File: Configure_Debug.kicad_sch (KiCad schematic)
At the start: 0 parts

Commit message: 更换电阻至新的结构
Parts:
- added CN5: 3020-10-0300-00-TR, MY_Connector_PH2.54:CONN_3020-10-0300-00-TR_CNC, symbol MY_Connector:3020-10-0300-00-TR
- added S1: 100mA 25VDC, MY_Switch:CK_SW_SD08H0SBR, symbol MY_Switch:SD08H0SBR
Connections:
- new net FULLPWRMGMTZ_SMBA1: S1.1
- new net GANGED_SMBA2_HS: S1.4
- new net PWRCTL_POL_TDO: S1.2
- new net PWRCTRL_BATEN1: S1.7
- new net PWRCTRL_BATEN2: S1.8
- new net SCL_SMBCLK: S1.5
- new net SDA_SMBDAT: S1.6
- new net SMBUSZ: S1.3

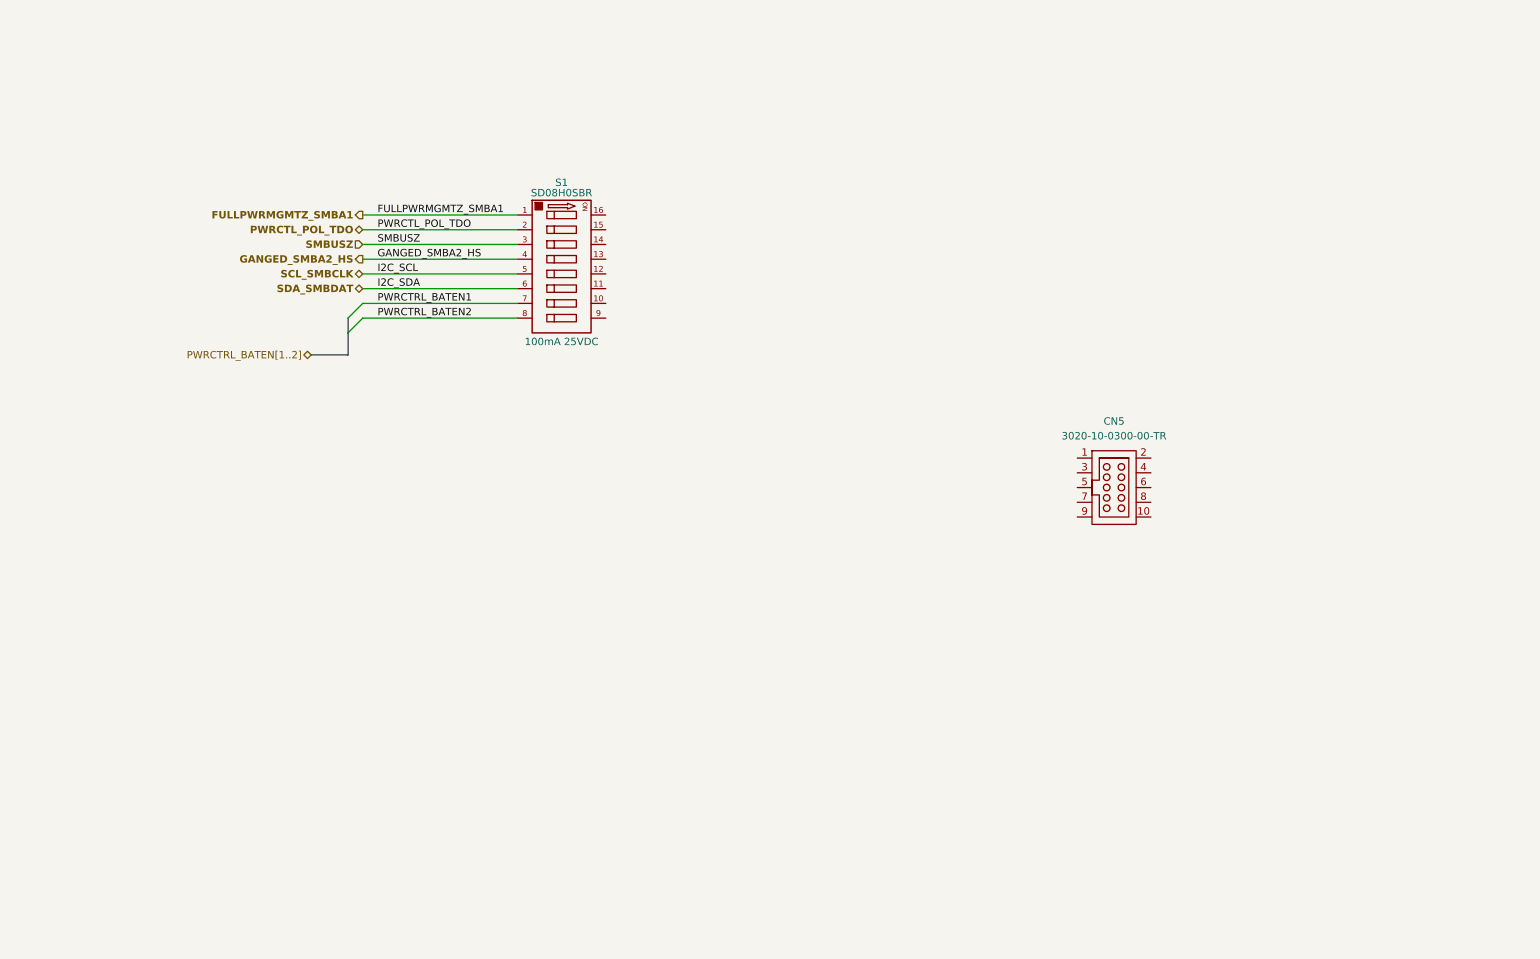
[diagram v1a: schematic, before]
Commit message: 完成电路原理图的绘制与批注
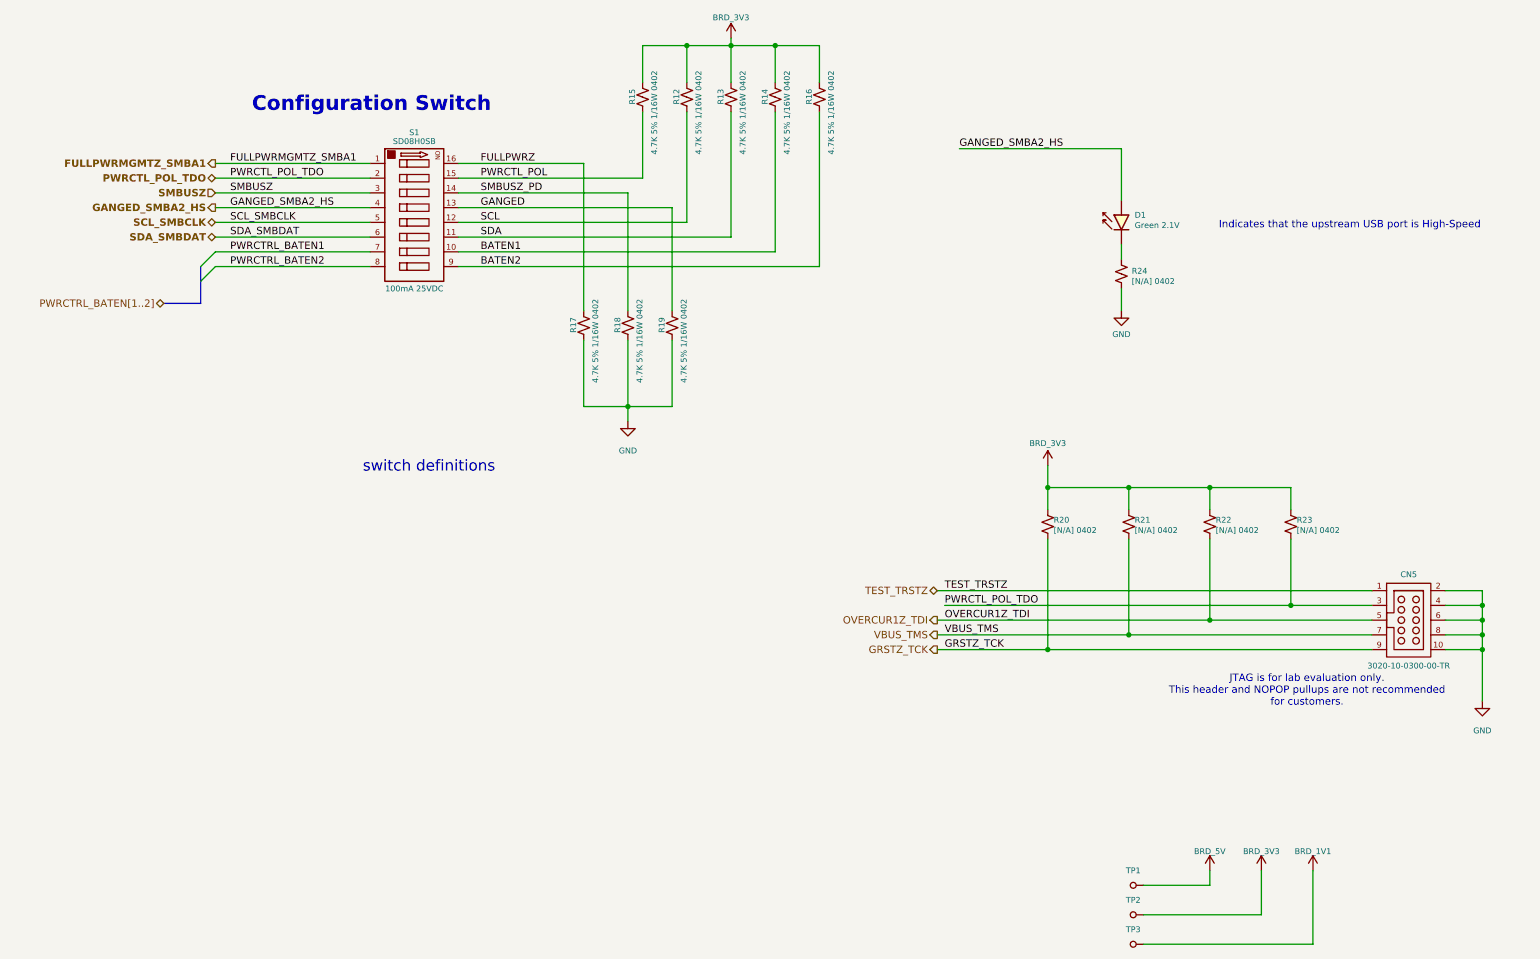
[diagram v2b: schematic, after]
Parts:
- removed CN5: 3020-10-0300-00-TR, MY_Connector_PH2.54:CONN_3020-10-0300-00-TR_CNC, symbol MY_Connector:3020-10-0300-00-TR
- removed S1: 100mA 25VDC, MY_Switch:CK_SW_SD08H0SBR, symbol MY_Switch:SD08H0SBR
- added CN5: 3020-10-0300-00-TR, MY_Connector_PH2.54:CONN_3020-10-0300-00-TR_CNC, symbol MY_CONN_PH2.54mm:3020-10-0300-00-TR
- added D1: Green 2.1V, MY_Led:LTST-C171, symbol MY_Led:LTST-C171GKT
- added R12, R13, R14, R15, R16, R17, R18, R19: 4.7K 5% 1/16W 0402, MY_Res:YAGEO_R0402, symbol MY_Res_YAGEO_AF:AF0402JR-074K7L
- added R20, R21, R22, R23, R24: [N/A] 0402, MY_Res:YAGEO_R0402, symbol MY_Res_YAGEO_AF:AF0402XXXXXXXXXL
- added S1: 100mA 25VDC, MY_Switch:CK_SW_SD08H0SB, symbol MY_Switch:SD08H0SB
- added TP1, TP2, TP3: ~, MY_Test:TP_Pad_D1.5mm, symbol MY_Test:TP_Pad_D1.5mm
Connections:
- net FULLPWRMGMTZ_SMBA1: now also S1.1
- net GANGED_SMBA2_HS: now also D1.2 (A), S1.4
- net PWRCTL_POL_TDO: now also CN5.3, R23.2, S1.2
- net PWRCTRL_BATEN1: now also S1.7
- net PWRCTRL_BATEN2: now also S1.8
- net SCL_SMBCLK: now also S1.5
- net SDA_SMBDAT: now also S1.6
- net SMBUSZ: now also S1.3
- new net: D1.1 (K), R24.1
- new net BATEN1: R14.2, S1.10
- new net BATEN2: R16.2, S1.9
- new net BRD_1V1: TP3.1
- new net BRD_3V3: R12.1, R13.1, R14.1, R15.1, R16.1, R20.1, R21.1, R22.1, R23.1, TP2.1
- new net BRD_5V: TP1.1
- new net FULLPWRZ: R17.1, S1.16
- new net GANGED: R19.1, S1.13
- new net GND: CN5.10, CN5.2, CN5.4, CN5.6, CN5.8, R17.2, R18.2, R19.2, R24.2
- new net GRSTZ_TCK: CN5.9, R20.2
- new net OVERCUR1Z_TDI: CN5.5, R22.2
- new net PWRCTL_POL: R15.2, S1.15
- new net SCL: R12.2, S1.12
- new net SDA: R13.2, S1.11
- new net SMBUSZ_PD: R18.1, S1.14
- new net TEST_TRSTZ: CN5.1
- new net VBUS_TMS: CN5.7, R21.2
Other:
- note added: "Configuration Switch"
- note added: "Indicates that the upstream USB port is High-Speed"
- note added: "JTAG is for lab evaluation only. This header and NOPOP pullups are not recommended for customers."
- note added: "switch definitions"
- company: (none) -> RICKY
- title: (none) -> Configure and Debug

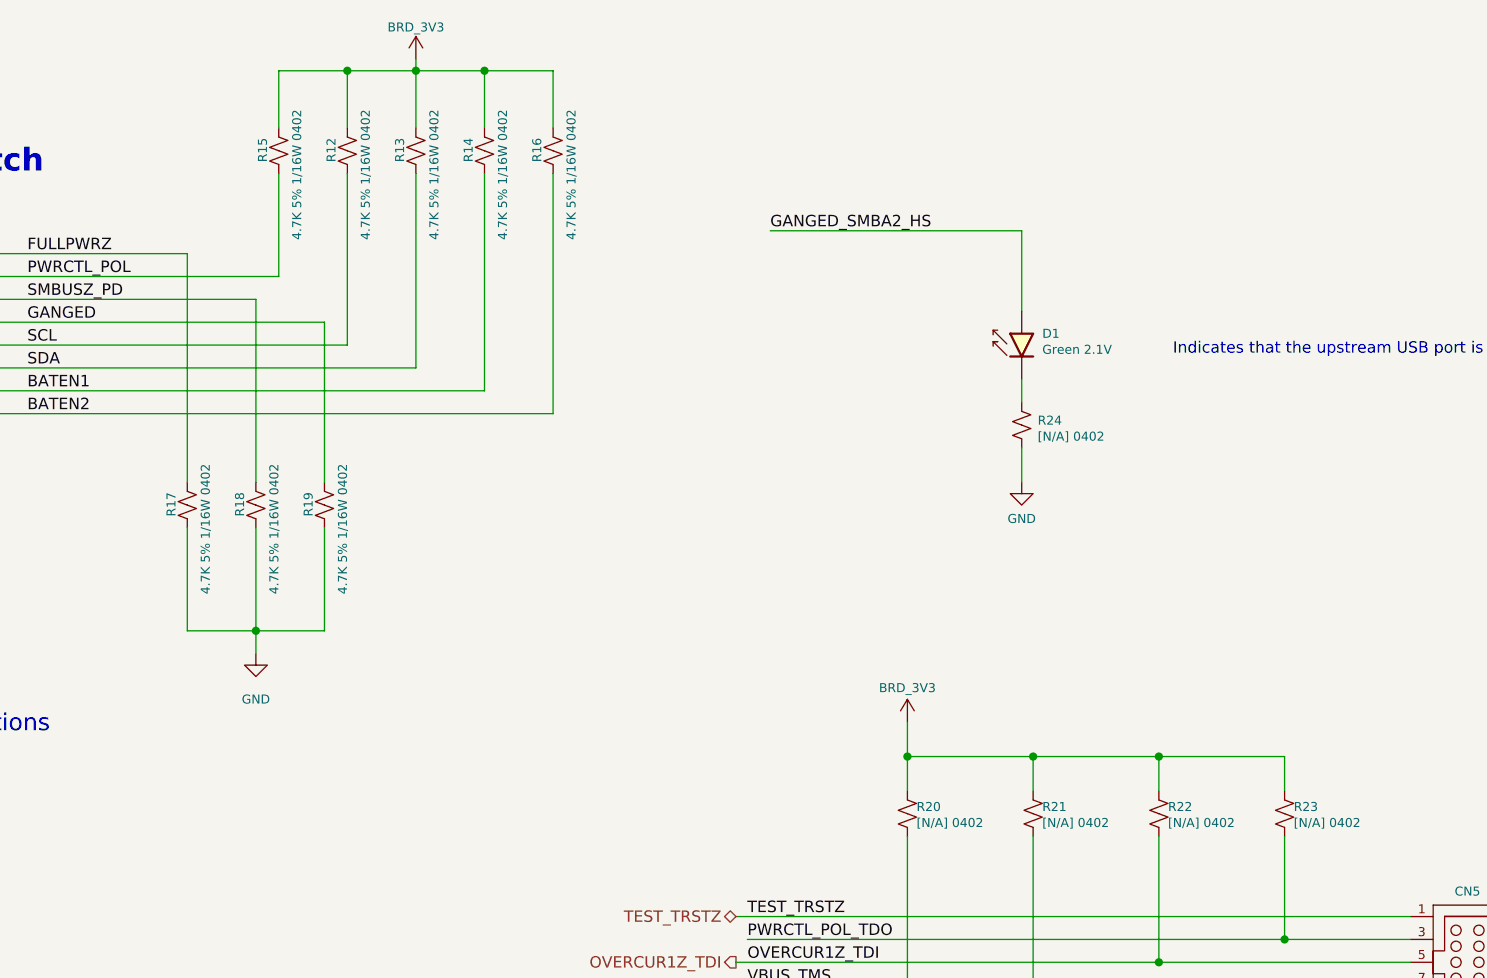
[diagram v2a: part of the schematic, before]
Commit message: 1. 原理图添加定位孔 2. PCB 设置基础参数，网络分类，预设间距线宽
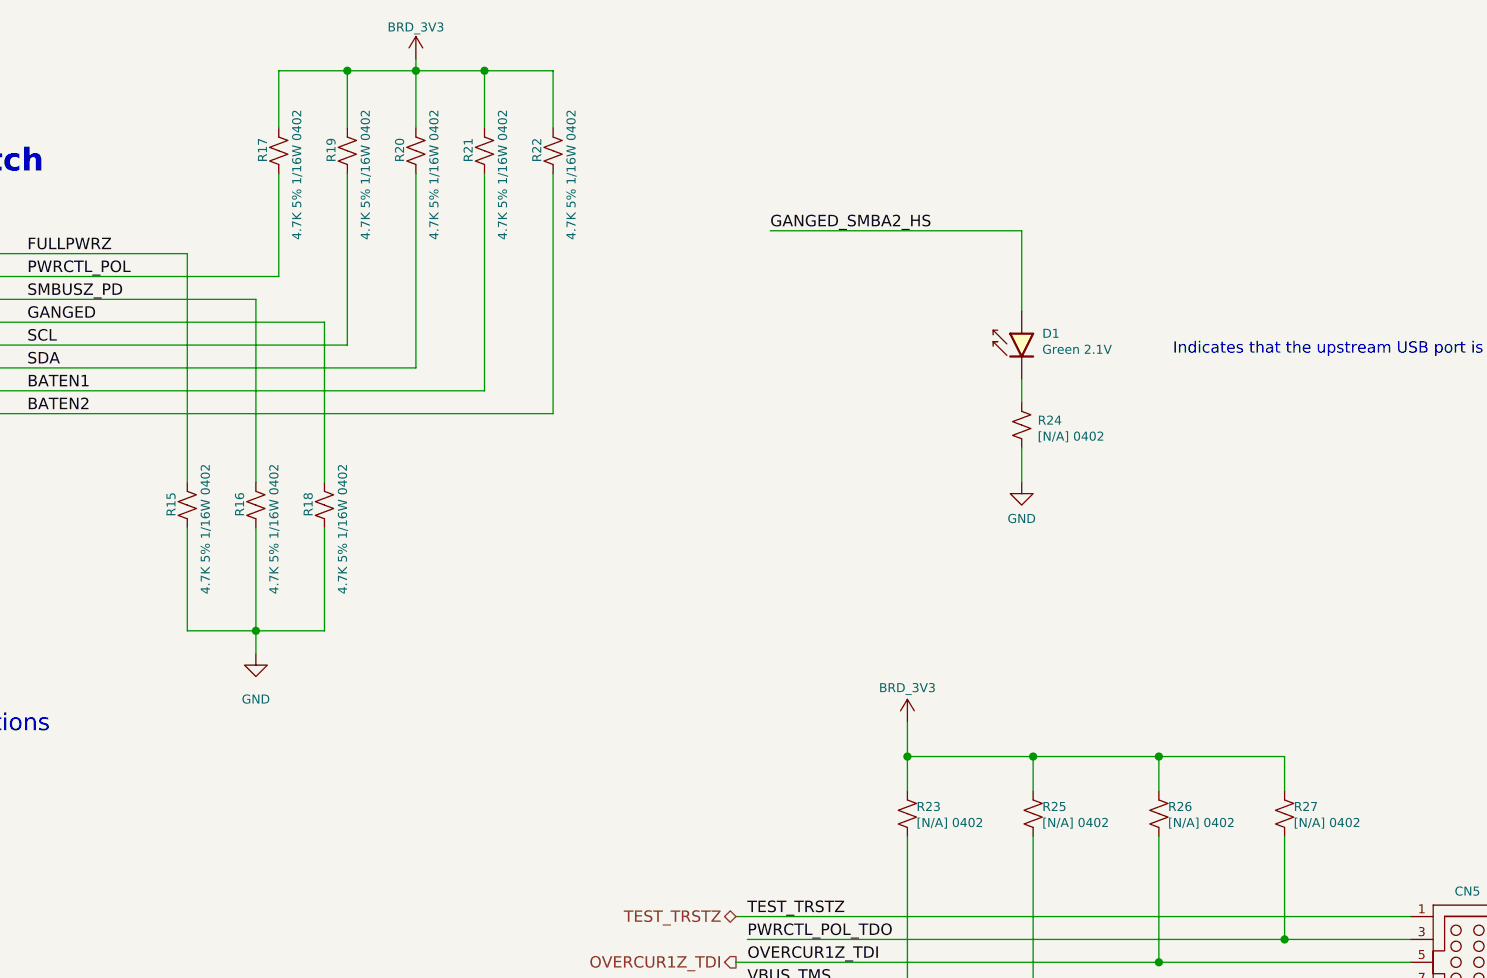
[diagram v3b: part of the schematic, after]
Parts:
- CN5: footprint MY_Connector_PH2.54:CONN_3020-10-0300-00-TR_CNC -> MY_Connector_PH2.54:CNC_302010030000TR
- renumbered R17 to R15, R18 to R16, R15 to R17, R19 to R18, R12 to R19, R13 to R20, R14 to R21, R16 to R22, R20 to R23, R21 to R25, R22 to R26, R23 to R27
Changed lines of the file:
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@@
 		(on_board yes)
 		(dnp no)
-		(property "Reference" "R14"
+		(property "Reference" "R21"
 			(at 144.272 33.02 90)
 			(effects
@@
 			(project "USBHub"
 				(path "/07e28d9d-adcb-473d-a362-1ef0c979820d/150922e4-fdd8-4f23-80c4-730d3fbf126a"
-					(reference "R14")
+					(reference "R21")
 					(unit 1)
 				)
@@
 		(on_board yes)
 		(dnp no)
-		(property "Reference" "R16"
+		(property "Reference" "R22"
 			(at 151.892 33.02 90)
 			(effects
@@
 			(project "USBHub"
 				(path "/07e28d9d-adcb-473d-a362-1ef0c979820d/150922e4-fdd8-4f23-80c4-730d3fbf126a"
-					(reference "R16")
+					(reference "R22")
 					(unit 1)
 				)
@@
 		(on_board yes)
 		(dnp no)
-		(property "Reference" "R21"
+		(property "Reference" "R25"
 			(at 208.026 104.648 0)
 			(effects
@@
 			(project "USBHub"
 				(path "/07e28d9d-adcb-473d-a362-1ef0c979820d/150922e4-fdd8-4f23-80c4-730d3fbf126a"
-					(reference "R21")
+					(reference "R25")
 					(unit 1)
 				)
@@
 		(on_board yes)
 		(dnp no)
-		(property "Reference" "#PWR23"
+		(property "Reference" "#PWR043"
 			(at 138.43 33.528 0)
 			(effects
@@
 			(project ""
 				(path "/07e28d9d-adcb-473d-a362-1ef0c979820d/150922e4-fdd8-4f23-80c4-730d3fbf126a"
-					(reference "#PWR23")
+					(reference "#PWR043")
 					(unit 1)
 				)
@@
 		(on_board yes)
 		(dnp no)
-		(property "Reference" "R12"
+		(property "Reference" "R19"
 			(at 129.032 33.02 90)
 			(effects
@@
 			(project "USBHub"
 				(path "/07e28d9d-adcb-473d-a362-1ef0c979820d/150922e4-fdd8-4f23-80c4-730d3fbf126a"
-					(reference "R12")
+					(reference "R19")
 					(unit 1)
 				)
@@
 		(on_board yes)
 		(dnp no)
-		(property "Reference" "R15"
+		(property "Reference" "R17"
 			(at 121.412 33.02 90)
 			(effects
@@
 			(project "USBHub"
 				(path "/07e28d9d-adcb-473d-a362-1ef0c979820d/150922e4-fdd8-4f23-80c4-730d3fbf126a"
-					(reference "R15")
+					(reference "R17")
 					(unit 1)
 				)
@@
 		(dnp no)
 		(fields_autoplaced yes)
-		(property "Reference" "#PWR24"
+		(property "Reference" "#PWR042"
 			(at 120.65 93.98 0)
 			(effects
@@
 			(project ""
 				(path "/07e28d9d-adcb-473d-a362-1ef0c979820d/150922e4-fdd8-4f23-80c4-730d3fbf126a"
-					(reference "#PWR24")
+					(reference "#PWR042")
 					(unit 1)
 				)
@@
 		(on_board yes)
 		(dnp no)
-		(property "Reference" "R22"
+		(property "Reference" "R26"
 			(at 221.996 104.648 0)
 			(effects
@@
 			(project "USBHub"
 				(path "/07e28d9d-adcb-473d-a362-1ef0c979820d/150922e4-fdd8-4f23-80c4-730d3fbf126a"
-					(reference "R22")
+					(reference "R26")
 					(unit 1)
 				)
@@
 		(on_board yes)
 		(dnp no)
-		(property "Reference" "#PWR060"
+		(property "Reference" "#PWR046"
 			(at 220.98 177.038 0)
 			(effects
@@
 			(project "USBHub"
 				(path "/07e28d9d-adcb-473d-a362-1ef0c979820d/150922e4-fdd8-4f23-80c4-730d3fbf126a"
-					(reference "#PWR060")
+					(reference "#PWR046")
 					(unit 1)
 				)
@@
 		(dnp no)
 		(fields_autoplaced yes)
-		(property "Reference" "#PWR25"
+		(property "Reference" "#PWR049"
 			(at 267.97 142.24 0)
 			(effects
@@
 			(project "USBHub"
 				(path "/07e28d9d-adcb-473d-a362-1ef0c979820d/150922e4-fdd8-4f23-80c4-730d3fbf126a"
-					(reference "#PWR25")
+					(reference "#PWR049")
 					(unit 1)
 				)
@@
 		(on_board yes)
 		(dnp no)
-		(property "Reference" "#PWR061"
+		(property "Reference" "#PWR047"
 			(at 229.87 177.038 0)
 			(effects
@@
 			(project "USBHub"
 				(path "/07e28d9d-adcb-473d-a362-1ef0c979820d/150922e4-fdd8-4f23-80c4-730d3fbf126a"
-					(reference "#PWR061")
+					(reference "#PWR047")
 					(unit 1)
 				)
@@
 		(on_board yes)
 		(dnp no)
-		(property "Reference" "R17"
+		(property "Reference" "R15"
 			(at 111.252 72.39 90)
 			(effects
@@
 			(project "USBHub"
 				(path "/07e28d9d-adcb-473d-a362-1ef0c979820d/150922e4-fdd8-4f23-80c4-730d3fbf126a"
-					(reference "R17")
+					(reference "R15")
 					(unit 1)
 				)
@@
 		(on_board yes)
 		(dnp no)
-		(property "Reference" "R19"
+		(property "Reference" "R18"
 			(at 126.492 72.39 90)
 			(effects
@@
 			(project "USBHub"
 				(path "/07e28d9d-adcb-473d-a362-1ef0c979820d/150922e4-fdd8-4f23-80c4-730d3fbf126a"
-					(reference "R19")
+					(reference "R18")
 					(unit 1)
 				)
@@
 		(on_board yes)
 		(dnp no)
-		(property "Reference" "#PWR27"
+		(property "Reference" "#PWR045"
 			(at 205.74 74.93 0)
 			(effects
@@
 			(project ""
 				(path "/07e28d9d-adcb-473d-a362-1ef0c979820d/150922e4-fdd8-4f23-80c4-730d3fbf126a"
-					(reference "#PWR27")
+					(reference "#PWR045")
 					(unit 1)
 				)
@@
 		(on_board yes)
 		(dnp no)
-		(property "Reference" "#PWR26"
+		(property "Reference" "#PWR044"
 			(at 193.04 107.188 0)
 			(effects
@@
 			(project ""
 				(path "/07e28d9d-adcb-473d-a362-1ef0c979820d/150922e4-fdd8-4f23-80c4-730d3fbf126a"
-					(reference "#PWR26")
+					(reference "#PWR044")
 					(unit 1)
 				)
@@
 		(on_board yes)
 		(dnp no)
-		(property "Reference" "R23"
+		(property "Reference" "R27"
 			(at 235.966 104.648 0)
 			(effects
@@
 			(project "USBHub"
 				(path "/07e28d9d-adcb-473d-a362-1ef0c979820d/150922e4-fdd8-4f23-80c4-730d3fbf126a"
-					(reference "R23")
+					(reference "R27")
 					(unit 1)
 				)
@@
 		(on_board yes)
 		(dnp no)
-		(property "Reference" "R18"
+		(property "Reference" "R16"
 			(at 118.872 72.39 90)
 			(effects
@@
 			(project "USBHub"
 				(path "/07e28d9d-adcb-473d-a362-1ef0c979820d/150922e4-fdd8-4f23-80c4-730d3fbf126a"
-					(reference "R18")
+					(reference "R16")
 					(unit 1)
 				)
@@
 			)
 		)
-		(property "Footprint" "MY_Connector_PH2.54:CONN_3020-10-0300-00-TR_CNC"
+		(property "Footprint" "MY_Connector_PH2.54:CNC_302010030000TR"
 			(at 255.27 132.588 0)
 			(effects
@@
 		(on_board yes)
 		(dnp no)
-		(property "Reference" "#PWR062"
+		(property "Reference" "#PWR048"
 			(at 238.76 177.038 0)
 			(effects
@@
 			(project "USBHub"
 				(path "/07e28d9d-adcb-473d-a362-1ef0c979820d/150922e4-fdd8-4f23-80c4-730d3fbf126a"
-					(reference "#PWR062")
+					(reference "#PWR048")
 					(unit 1)
 				)
@@
 		(on_board yes)
 		(dnp no)
-		(property "Reference" "R13"
+		(property "Reference" "R20"
 			(at 136.652 33.02 90)
 			(effects
@@
 			(project "USBHub"
 				(path "/07e28d9d-adcb-473d-a362-1ef0c979820d/150922e4-fdd8-4f23-80c4-730d3fbf126a"
-					(reference "R13")
+					(reference "R20")
 					(unit 1)
 				)
@@
 		(on_board yes)
 		(dnp no)
-		(property "Reference" "R20"
+		(property "Reference" "R23"
 			(at 194.056 104.648 0)
 			(effects
@@
 			(project ""
 				(path "/07e28d9d-adcb-473d-a362-1ef0c979820d/150922e4-fdd8-4f23-80c4-730d3fbf126a"
-					(reference "R20")
-					(unit 1)
-				)
+					(reference "R23")
+					(unit 1)
+				)
